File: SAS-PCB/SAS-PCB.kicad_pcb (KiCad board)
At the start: 2 copper layers, 76.2 x 76.2 mm, 25 parts, among them J10-FTDI1 Conn_01x06, J10-FTDI2 Conn_01x06, J1_Batt1 691137710002, J2-LCD1 Conn_01x04_Socket, J3-LCD2 Conn_01x04_Socket, J4-BMP280 Conn_01x06_Pin, J5-GPS1 Conn_01x04_Socket, J6-cable-plat1 Conn_02x20_Odd_Even, J7-RFD900x1 691137710002, J8-Fan1 Conn_01x04_Socket, J9-Fan2 Conn_01x04_Socket

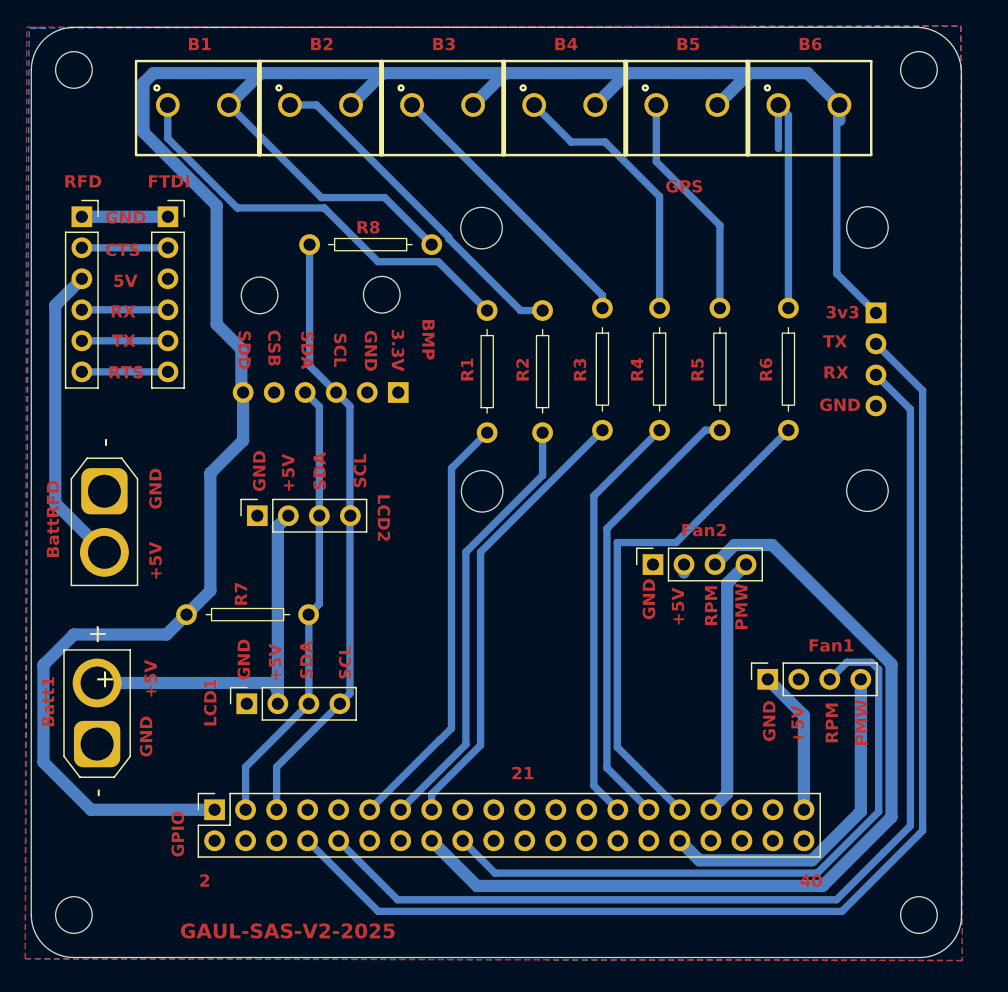
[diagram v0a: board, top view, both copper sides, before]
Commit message: Version_presque_fini
Trace fini avec via, augmentation de l'ecriture.  Il reste seulement les power plane pour 3.3V et 5V.
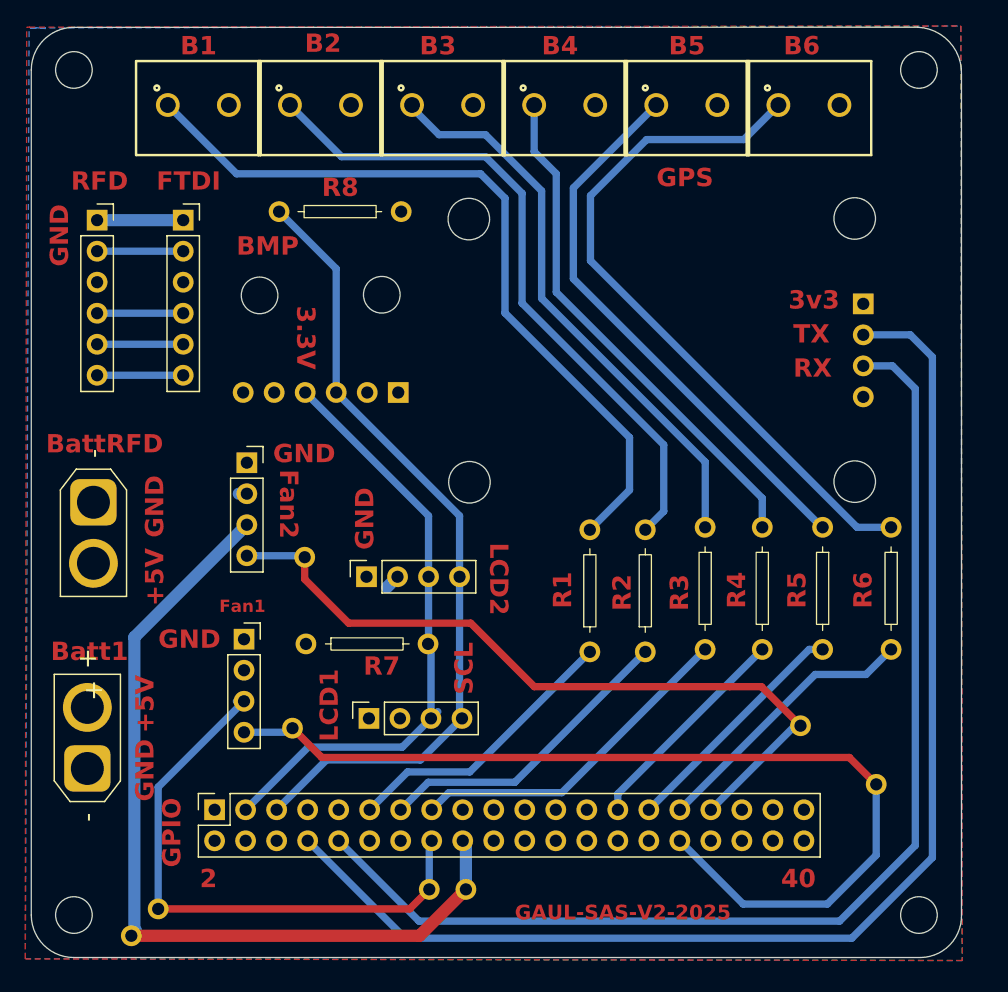
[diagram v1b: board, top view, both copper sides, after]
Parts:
- added ?: , , F.Cu at (68.2, 134.4)
- added ?: , , F.Cu at (129.2, 122.0)
- added ?: , , F.Cu at (81.4, 117.4)
- added ?: , , F.Cu at (70.4, 132.2)
- added ?: , , F.Cu at (82.4, 103.4)
- added ?: , , F.Cu at (95.6, 130.6)
- added ?: , , F.Cu at (92.6, 130.6)
- added ?: , , F.Cu at (123.0, 117.2)
- moved J8-Fan1 58.5 mm to (71.2, 119.5), turned to 0 degrees
- moved J9-Fan2 49.2 mm to (71.4, 105.1), turned to 0 degrees
- moved R1 19.8 mm to (105.8, 106.0)
- moved R2 19.8 mm to (110.4, 106.0)
- moved R3 19.8 mm to (115.1, 106.0)
- moved R4 19.8 mm to (119.8, 106.0)
- moved R5 19.8 mm to (124.7, 106.0)
- moved R6 19.8 mm to (130.3, 106.0)
- moved J3-LCD2 10.2 mm to (96.9, 111.2)
- moved J2-LCD1 10.1 mm to (97.1, 122.8)
- moved R7 10.1 mm to (87.6, 110.6)
- moved R8 3.68 mm to (85.2, 75.0)
- moved J1_Batt1 2.15 mm to (64.6, 120.7)
- moved J10-FTDI1 1.28 mm to (72.3, 93.2)
- moved J10-FTDI2 1.28 mm to (65.3, 93.2)
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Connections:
- J6-cable-plat1 pad 16: Fan2_RPM -> Fan1_RPM
- J6-cable-plat1 pad 18: Fan1_RPM -> Fan2_RPM
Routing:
- net +3.3V: track 203.7 -> 0.51 mm
- net +5V: track 58.8 -> 3.06 mm
- net Fan1_PWM: track 28.0 -> 79.5 mm
- net Fan2_PWM: track 21.3 -> 62.4 mm
- net Net-(Bouton_6-GND): track 20.5 -> 57.4 mm
- net Net-(Bouton_1-GND): track 34.7 -> 63.5 mm
- net Net-(Bouton_5-GND): track 18.8 -> 46.1 mm
- net Net-(Bouton_2-GND): track 27.7 -> 55.0 mm
- net Net-(Bouton_3-GND): track 23.1 -> 46.8 mm
- net Net-(Bouton_4-GND): track 22.5 -> 42.3 mm
- net Bouton_6: track 41.8 -> 22.7 mm
- net Bouton_5: track 37.0 -> 19.7 mm
- net SCL: track 50.2 -> 66.3 mm
- net Bouton_4: track 34.1 -> 18.0 mm
- net SDA: track 37.3 -> 50.2 mm
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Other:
- board text removed: "21"
- board text removed: "5V"
- board text removed: "CSB"
- board text removed: "CTS"
- board text removed: "PMW"
- board text removed: "RPM"
- board text removed: "RTS"
- board text removed: "SDA"
- board text removed: "SDD"

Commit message: Version_fini
Ajouter les zones: ground, 5V, 3V3
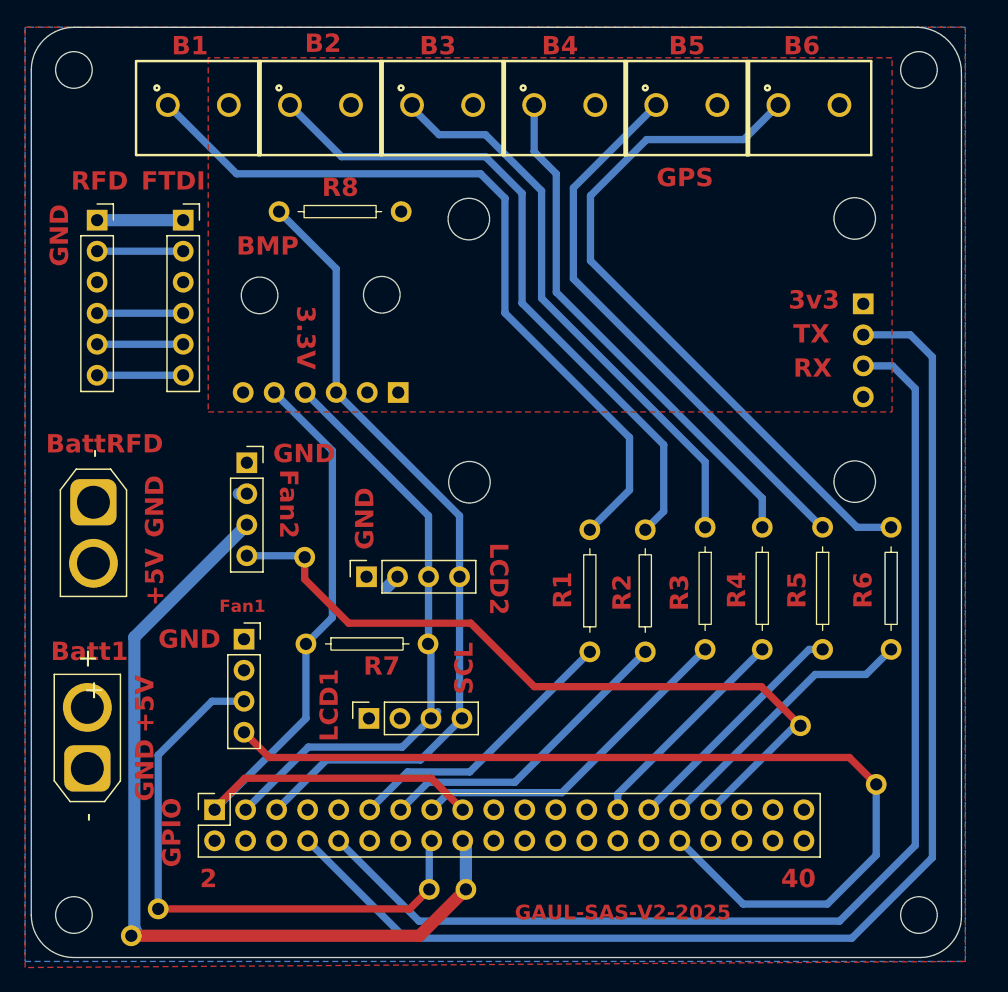
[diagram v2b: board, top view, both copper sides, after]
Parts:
- removed the ? at (81.4, 117.4)
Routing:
- net +3.3V: track 0.51 -> 63.1 mm
- net Fan1_RPM: track 47.5 -> 49.0 mm
- added copper zone on F.Cu, net +3.3V
- added copper zone on F.Cu, net +5V
- removed copper zone on F.Cu, net (none)
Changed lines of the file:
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@@
 		)
 	)
-	(footprint ""
-		(layer "F.Cu")
-		(at 81.4 117.4)
-		(property "Reference" ""
-			(at 0 0 0)
-			(layer "F.SilkS")
-			(effects
-				(font
-					(size 1.27 1.27)
-					(thickness 0.15)
-				)
-			)
-		)
-		(property "Value" ""
-			(at 0 0 0)
-			(layer "F.Fab")
-			(effects
-				(font
-					(size 1.27 1.27)
-					(thickness 0.15)
-				)
-			)
-		)
-		(property "Footprint" ""
-			(at 0 0 0)
-			(layer "F.Fab")
-			(hide yes)
-			(effects
-				(font
-					(size 1.27 1.27)
-					(thickness 0.15)
-				)
-			)
-		)
-		(property "Datasheet" ""
-			(at 0 0 0)
-			(layer "F.Fab")
-			(hide yes)
-			(effects
-				(font
-					(size 1.27 1.27)
-					(thickness 0.15)
-				)
-			)
-		)
-		(property "Description" ""
-			(at 0 0 0)
-			(layer "F.Fab")
-			(hide yes)
-			(effects
-				(font
-					(size 1.27 1.27)
-					(thickness 0.15)
-				)
-			)
-		)
-		(pad "v_f1_PMW" thru_hole oval
-			(at 0 0 90)
-			(size 1.7 1.7)
-			(drill 1)
-			(layers "*.Cu" "*.Mask")
-			(remove_unused_layers no)
-			(net 22 "Fan1_PWM")
-			(pinfunction "Pin_4")
-			(pintype "passive+no_connect")
-		)
-	)
 	(footprint "SAS-Librarie-Empreinte:AMASS_XT30U-F_1x02_P5.0mm_Vertical"
 		(layer "F.Cu")
@@
 	)
 	(gr_text "FTDI"
-		(at 70.25 73.48 0)
+		(at 69 73.48 0)
 		(layer "F.Cu" knockout)
 		(effects
@@
 	)
 	(gr_text "B1"
-		(at 72.2 62.4 0)
+		(at 71.5 62.4 0)
 		(layer "F.Cu" knockout)
 		(effects
@@
 	)
 	(segment
+		(start 75.02 123.98)
+		(end 77.5 121.5)
+		(width 0.6)
+		(layer "F.Cu")
+		(net 2)
+	)
+	(segment
+		(start 92.76 121.5)
+		(end 95.34 124.08)
+		(width 0.6)
+		(layer "F.Cu")
+		(net 2)
+	)
+	(segment
+		(start 77.5 121.5)
+		(end 92.76 121.5)
+		(width 0.6)
+		(layer "F.Cu")
+		(net 2)
+	)
+	(segment
+		(start 82.5 110.5)
+		(end 84.663959 108.336041)
+		(width 0.6)
+		(layer "B.Cu")
+		(net 2)
+	)
+	(segment
+		(start 84.663959 108.336041)
+		(end 84.663959 94.673959)
+		(width 0.6)
+		(layer "B.Cu")
+		(net 2)
+	)
+	(segment
+		(start 82.5 116.6)
+		(end 82.5 110.5)
+		(width 0.6)
+		(layer "B.Cu")
+		(net 2)
+	)
+	(segment
 		(start 125.97013 66.58987)
 		(end 126.19 66.37)
@@
 	)
 	(segment
+		(start 75.02 124.08)
+		(end 82.5 116.6)
+		(width 0.6)
+		(layer "B.Cu")
+		(net 2)
+	)
+	(segment
 		(start 77.36 89.91)
 		(end 77.216 89.766)
@@
 	)
 	(segment
+		(start 84.663959 94.673959)
+		(end 79.9 89.91)
+		(width 0.6)
+		(layer "B.Cu")
+		(net 2)
+	)
+	(segment
 		(start 85.42 70.6)
 		(end 81.19 66.37)
@@
 	)
 	(segment
-		(start 70.4 122.223888)
+		(start 74.805001 115.194999)
+		(end 70.4 119.6)
+		(width 0.6)
+		(layer "B.Cu")
+		(net 15)
+	)
+	(segment
+		(start 70.4 119.6)
 		(end 70.4 132.2)
 		(width 0.6)
@@
 	(segment
 		(start 77.428889 115.194999)
-		(end 70.4 122.223888)
+		(end 74.805001 115.194999)
 		(width 0.6)
 		(layer "B.Cu")
@@
 	)
 	(segment
-		(start 83.8 119.8)
-		(end 81.4 117.4)
+		(start 127 119.8)
+		(end 79.49389 119.8)
 		(width 0.6)
 		(layer "F.Cu")
@@
 	)
 	(segment
-		(start 127 119.8)
-		(end 83.8 119.8)
+		(start 79.49389 119.8)
+		(end 77.428889 117.734999)
 		(width 0.6)
 		(layer "F.Cu")
@@
 	)
 	(segment
-		(start 77.428889 117.734999)
-		(end 81.065001 117.734999)
-		(width 0.6)
-		(layer "B.Cu")
-		(net 22)
-	)
-	(segment
 		(start 118.3 131.8)
 		(end 113.12 126.62)
@@
 	)
 	(segment
-		(start 81.065001 117.734999)
-		(end 81.4 117.4)
-		(width 0.6)
-		(layer "B.Cu")
-		(net 22)
-	)
-	(segment
 		(start 129.2 122)
 		(end 129.2 127.8)
@@
 	)
 	(zone
-		(net 0)
-		(net_name "")
+		(net 2)
+		(net_name "+3.3V")
+		(layer "F.Cu")
+		(hatch edge 0.5)
+		(priority 2)
+		(connect_pads
+			(clearance 0)
+		)
+		(min_thickness 0.25)
+		(filled_areas_thickness no)
+		(fill yes
+			(thermal_gap 0.5)
+			(thermal_bridge_width 0.5)
+			(island_removal_mode 1)
+			(island_area_min 10)
+		)
+		(polygon
+			(pts
+				(xy 74.5 62.5) (xy 74.5 91.5) (xy 130.5 91.5) (xy 130.5 62.5)
+			)
+		)
+	)
+	(zone
+		(net 8)
+		(net_name "+5V")
 		(layer "F.Cu")
 		(hatch edge 0.5)
@@
 		(polygon
 			(pts
-				(xy 59.8424 59.9948) (xy 136.144 59.8932) (xy 136.2456 136.4234) (xy 59.5122 136.2964) (xy 59.6392 59.9948)
-				(xy 59.8678 59.9948)
+				(xy 59.5 60) (xy 136.5 60) (xy 136.5 136.5) (xy 59.5 137)
 			)
 		)
@@
 			(thermal_gap 0.5)
 			(thermal_bridge_width 0.5)
+			(island_removal_mode 1)
+			(island_area_min 10)
 		)
 		(polygon
 			(pts
-				(xy 59.92 60.06) (xy 136.13 59.9) (xy 136.25 136.43) (xy 59.52 136.28) (xy 59.83 60.02) (xy 60.2 60.02)
-				(xy 61.2 60.1)
+				(xy 136.5 136.5) (xy 136.5 60) (xy 59.5 60) (xy 59.5 136.5)
 			)
 		)

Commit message: Modification de trace 3.3V
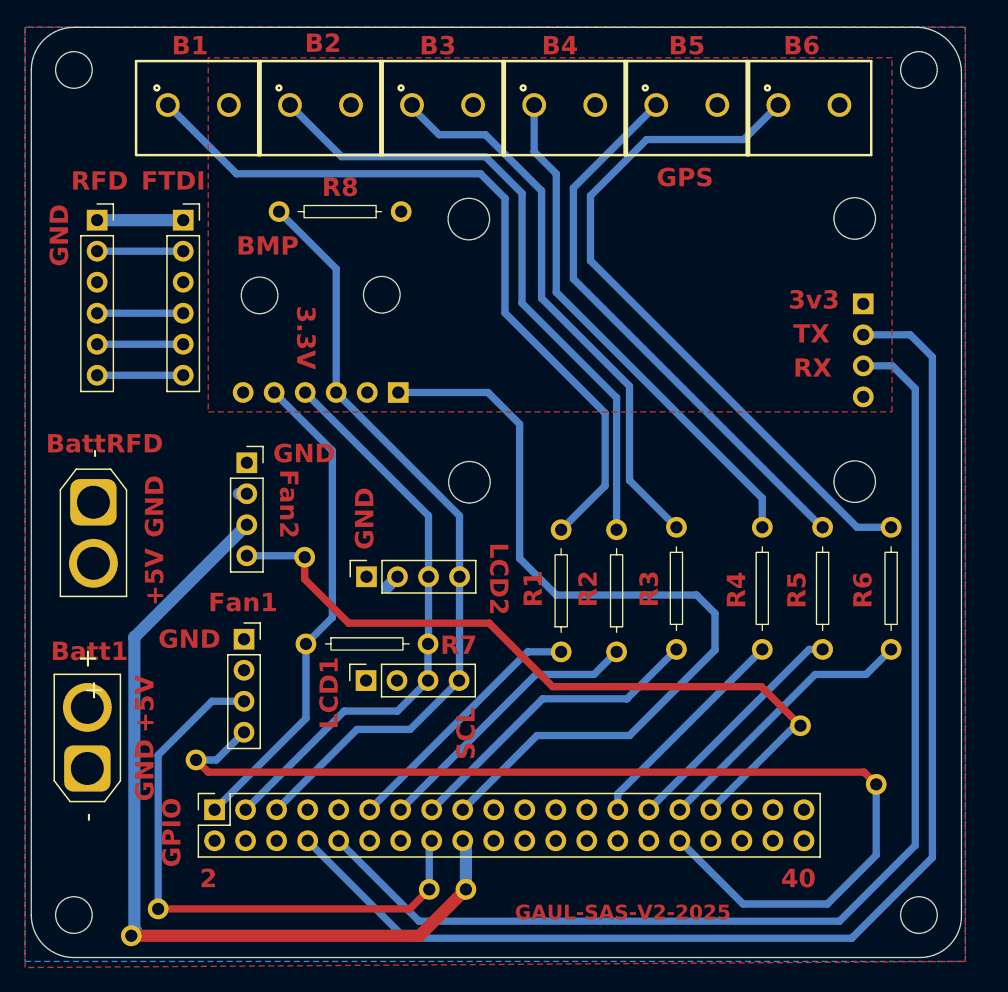
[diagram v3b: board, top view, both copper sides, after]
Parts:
- added ?: , , F.Cu at (73.5, 120.0)
- moved J2-LCD1 3.11 mm to (96.8, 119.8)
- moved R3 2.35 mm to (112.7, 106.0)
- moved R1 2.35 mm to (103.5, 106.0)
- moved R2 2.35 mm to (108.0, 106.0)
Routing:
- net +3.3V: track 63.1 -> 109.6 mm
- net Fan1_PWM: track 79.2 -> 87.4 mm
- net Bouton_3: track 28.4 -> 25.5 mm
- net SDA: track 50.2 -> 47.6 mm
- net Bouton_2: track 25.4 -> 23.0 mm
- net Bouton_1: track 23.4 -> 21.0 mm
- net Net-(Bouton_2-GND): track 55.0 -> 52.8 mm
- net SCL: track 66.3 -> 64.2 mm
- net Net-(Bouton_3-GND): track 46.8 -> 45.8 mm
- net Net-(Bouton_1-GND): track 63.5 -> 62.8 mm

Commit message: A_verifier_demain
Abandon du RPM tachymetre pour le mieux.
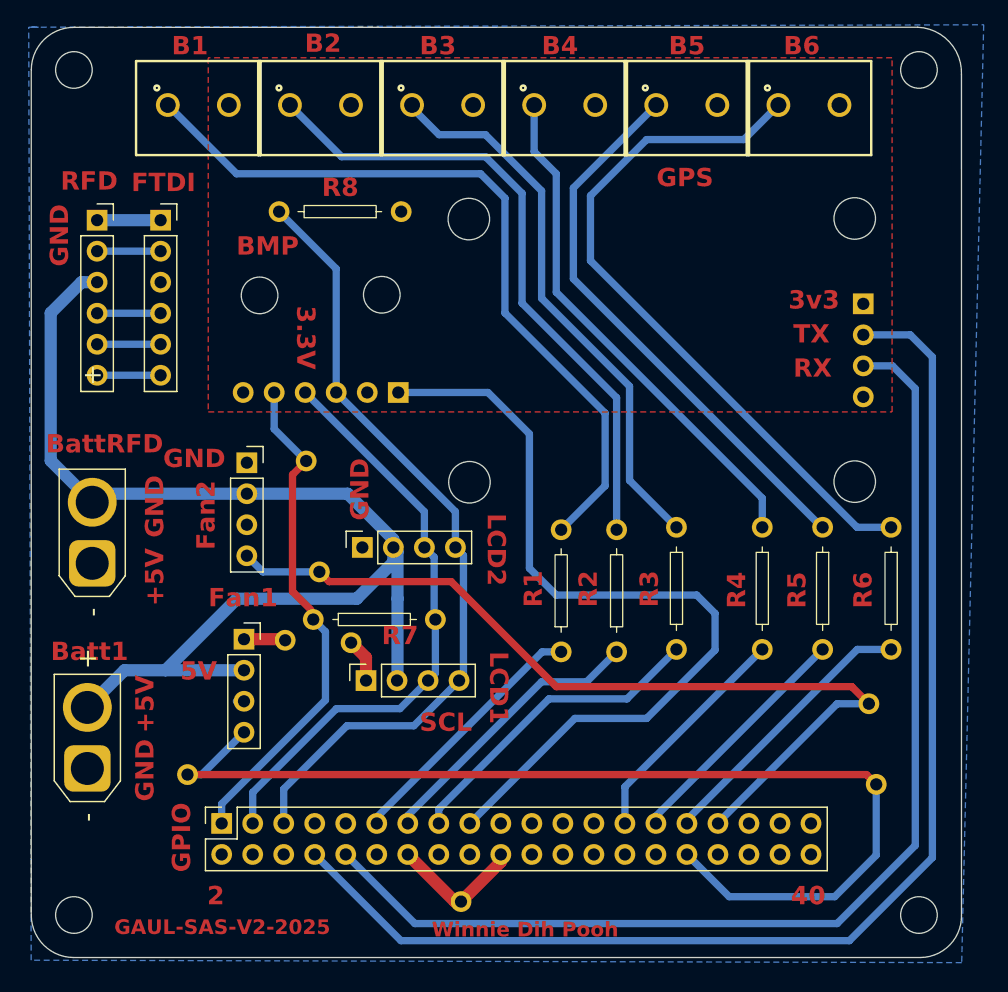
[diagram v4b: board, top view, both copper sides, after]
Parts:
- removed the ? at (68.2, 134.4)
- removed the ? at (70.4, 132.2)
- removed the ? at (95.6, 130.6)
- removed the ? at (92.6, 130.6)
- added 3.3V: , , B.Cu at (82.5, 95.5)
- added ?: , , F.Cu at (86.2, 110.4)
- added ?: , , F.Cu at (80.8, 110.2)
- added ?: , , F.Cu at (95.2, 131.6)
- moved ? 5.88 mm to (128.6, 115.4)
- moved J7-RFD900x1 5.00 mm to (65.0, 103.9), turned to 90 degrees
- moved J3-LCD2 2.42 mm to (96.5, 108.8)
- moved R7 2.09 mm to (88.2, 108.6)
- moved J10-FTDI1 1.85 mm to (70.5, 93.2)
- moved ? 1.70 mm to (83.6, 104.6)
- moved ? 1.39 mm to (72.8, 121.2)
- moved J6-cable-plat1 1.26 mm to (75.6, 125.2)
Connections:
- J6-cable-plat1 pad 16: Fan1_RPM -> Fan1_TACH_R
- J6-cable-plat1 pad 18: Fan2_RPM -> Fan2_TACH_R
- J8-Fan1 pad 3: Fan1_RPM -> Fan1_TACH
- J9-Fan2 pad 3: Fan2_RPM -> Fan2_TACH
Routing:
- net +5V: track 3.06 -> 97.9 mm
- net Fan2_RPM: track 71.2 -> 0.00 mm
- net Fan1_RPM: track 49.0 -> 0.00 mm
- net GND: track 8.29 -> 25.5 mm
- net Fan2_PWM: track 62.4 -> 72.4 mm
- net RFD_TX: track 7.05 -> 5.20 mm
- net RFD_RX: track 7.05 -> 5.20 mm
- net RFD_RTS: track 7.05 -> 5.20 mm
- net RFD_CTS: track 7.05 -> 5.40 mm
- net SDA: track 47.6 -> 49.1 mm
- net SCL: track 64.2 -> 65.7 mm
- net +3.3V: track 109.6 -> 110.5 mm
- net Bouton_4: track 18.0 -> 18.9 mm
- net TXD: track 104.7 -> 103.8 mm
- net RXD: track 94.9 -> 94.1 mm
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- removed copper zone on F.Cu, net +5V
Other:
- board text added: "5V"
- board text added: "Winnie Dih Pooh"

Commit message: Version_2_final
Version envoyer en impression
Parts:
- removed the ? at (95.2, 131.6)
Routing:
- net +3.3V: track 110.5 -> 274.5 mm
- net GND: track 25.5 -> 19.9 mm
- added copper zone on F.Cu, net (none)
- removed copper zone on F.Cu, net +3.3V
